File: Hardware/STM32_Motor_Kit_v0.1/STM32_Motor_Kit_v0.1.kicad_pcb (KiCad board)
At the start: 4 copper layers, 150 x 100 mm, 376 parts, among them J1 Conn_01x02_Male, J2 Conn_02x04_Odd_Even, J3 Conn_01x02_Male, J4 Conn_01x03_Male, J5 Conn_01x05_Male, J6 Conn_02x09_Odd_Even, J7 Conn_01x02_Male, J8 USB_B_Mini, Q1 NTMFS4119NT1G, Q2 NTMFS4119NT1G, Q3 NTMFS4119NT1G, Q4 NTMFS4119NT1G, Q5 NTMFS4119NT1G, Q6 NTMFS4119NT1G, Q7 MMUN2235LT1G, SW1 SW_DIP_x01, SW2 Push_Button_SMD_4P, SW3 Push_Button_SMD_4P, U1 STM32G431RBT6, U10 LMV358IDRG4, U11 LMV358IDRG4, U12 LMV358IDRG4, U13 LSF0204DPWR, U14 THVD1500D, U15 SN74HC595DRG3, U16 M24C64-WMN6TP, U17 TVS_Diode_USB, U2 AMS111733TR-HT, U3 LMV358IDRG4, U4 TPS54331DR, U5 MC78M15CDTRKG-, U6 TJA1441BT_0Z, U7 IR2104STRPBF, U8 IR2104STRPBF, U9 IR2104STRPBF, Y1 CRYSTAL_8mHz

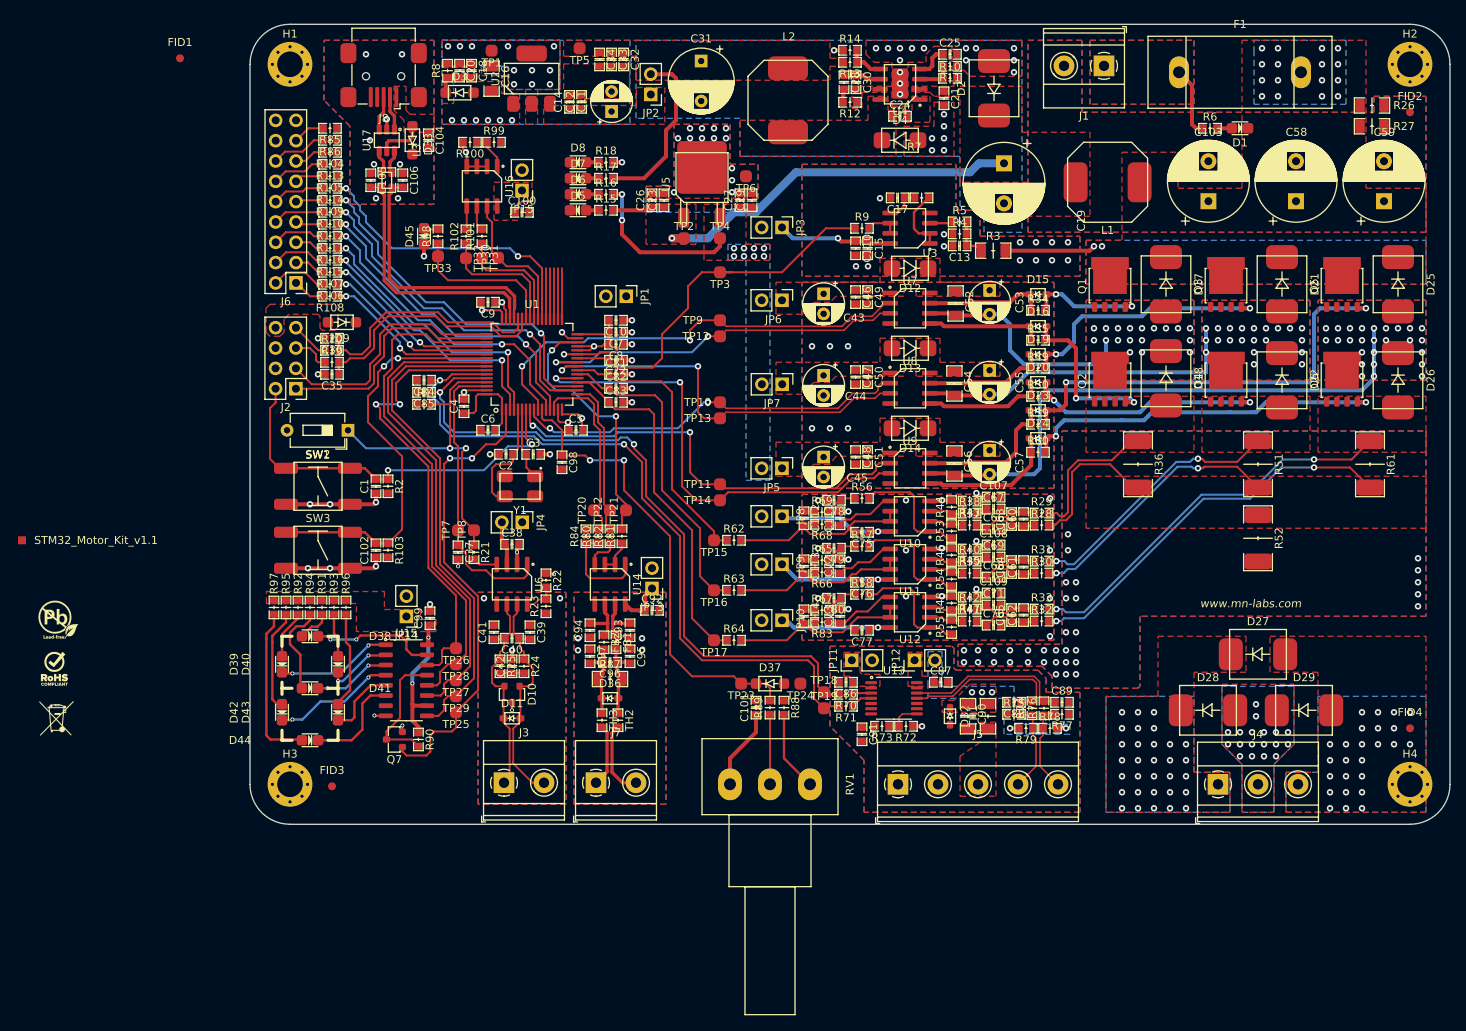
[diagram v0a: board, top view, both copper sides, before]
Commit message: 26.08.2024
1nF 2KV chassis ile GND arasına ekledim. PCB'de güncellemeler oldu.
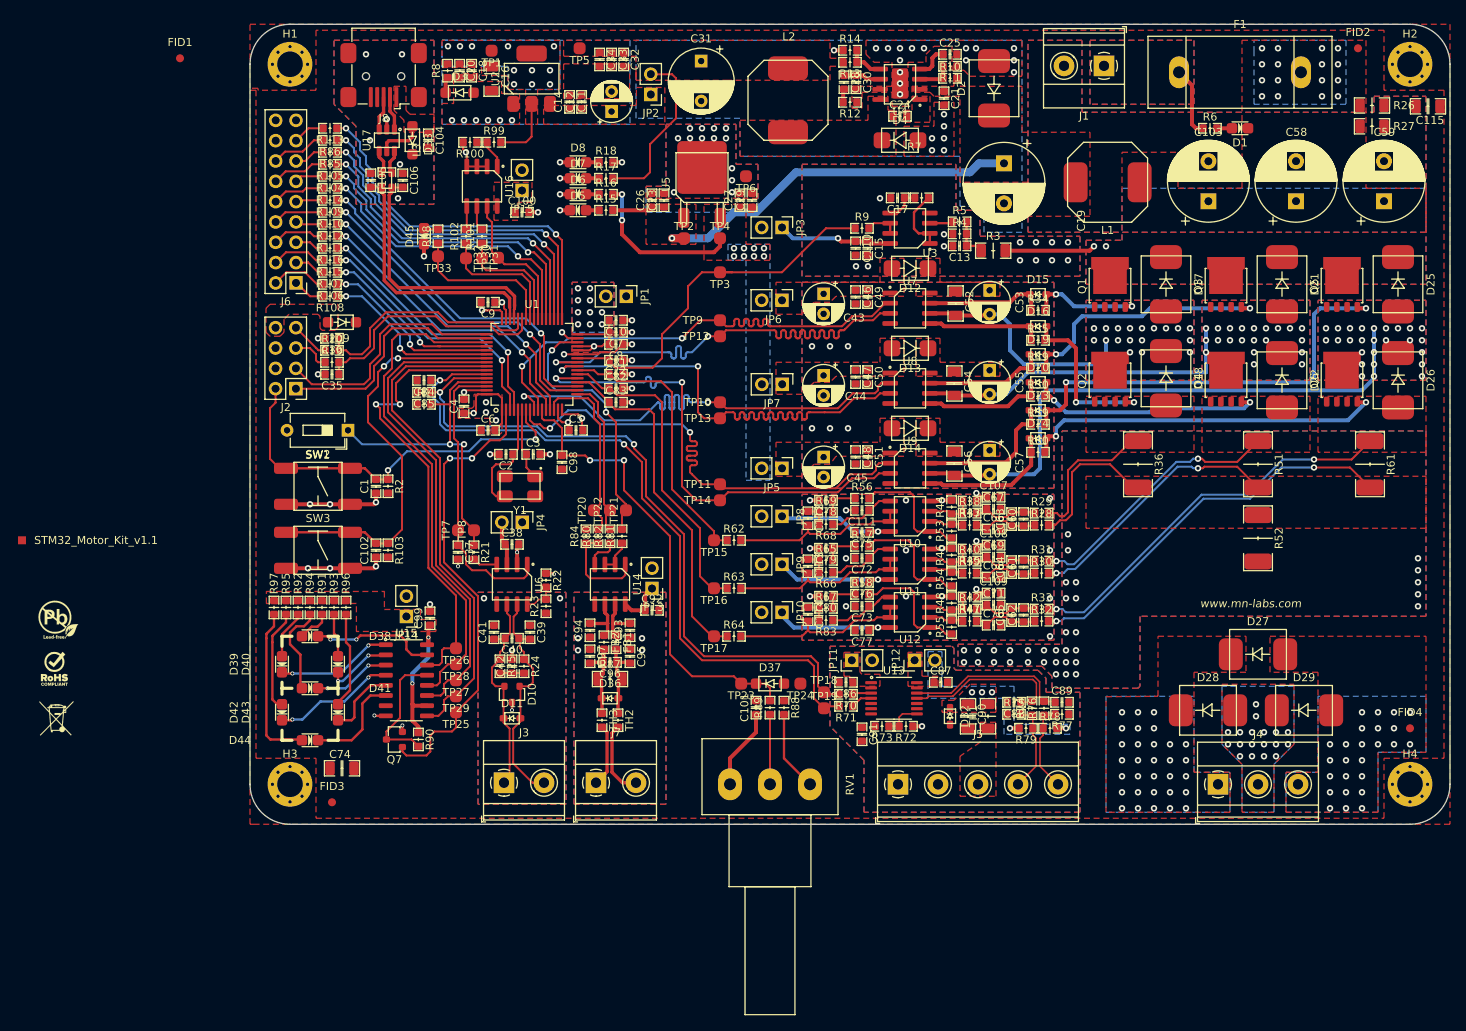
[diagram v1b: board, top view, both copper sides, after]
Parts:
- added C115: 1nF_2KV, AKE_Capacitor_SMD:CAP_1206, F.Cu at (197.2, 60.2)
- added C74: 1nF_2KV, AKE_Capacitor_SMD:CAP_1206, F.Cu at (61.5, 143.0)
- moved FID2 10.3 mm to (188.5, 53.0)
- moved R113 4.50 mm to (60.0, 63.0)
- moved C73 3.02 mm to (126.5, 122.8), turned to 180 degrees
- moved R104 3.00 mm to (60.0, 69.0)
- moved R85 3.00 mm to (60.0, 66.0)
- moved C111 2.93 mm to (126.5, 110.8), turned to 180 degrees
- moved C72 2.93 mm to (126.5, 116.8), turned to 180 degrees
- moved FID3 2.00 mm to (60.2, 147.2)
- moved R105 1.50 mm to (60.0, 67.5)
- moved C80 1.03 mm to (122.0, 121.5)
- moved C78 1.00 mm to (122.0, 109.5)
- moved C79 1.00 mm to (122.0, 115.5)
- moved JP10 1.00 mm to (116.5, 123.5)
- moved C114 0.56 mm to (119.8, 123.8)
- moved R67 0.56 mm to (122.0, 123.0)
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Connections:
- H1 pad 1: unconnected-(H1-Pad1) -> Chassis
- H2 pad 1: unconnected-(H2-Pad1) -> Chassis
- H3 pad 1: unconnected-(H3-Pad1) -> Chassis
- H4 pad 1: unconnected-(H4-Pad1) -> Chassis
- R104 pad 2: /GPIO/Pin_13 -> /GPIO/Pin_11
- R105 pad 1: /MCU/PB12 -> /MCU/PB14
- R105 pad 2: /GPIO/Pin_11 -> /GPIO/Pin_12
- R113 pad 2: /GPIO/Pin_12 -> /GPIO/Pin_15
- R85 pad 2: /GPIO/Pin_15 -> /GPIO/Pin_13
- R86 pad 1: /MCU/PB14 -> /MCU/PB12
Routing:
- net /MCU/PB11: track 6.33 -> 46.3 mm, vias 0 -> 2
- net /MCU/PB12: track 6.33 -> 44.3 mm, vias 0 -> 2
- net /MCU/PB13: track 6.33 -> 42.1 mm, vias 0 -> 2
- net /MCU/PB14: track 6.33 -> 40.3 mm, vias 0 -> 2
- net /MCU/PB15: track 6.33 -> 38.5 mm, vias 0 -> 2
- net /U_Drive_L: track 47.0 -> 61.6 mm
- net /V_Drive_H: track 49.6 -> 61.8 mm
- net /V_Drive_L: track 50.7 -> 61.6 mm
- net +3.3V: track 19.9 -> 28.1 mm
- net /W_Drive_H: track 56.2 -> 61.8 mm
- net /U_Drive_H: track 57.1 -> 61.8 mm
- net GND: track 91.5 -> 95.5 mm, vias 155 -> 158
- net /W_Drive_L: track 59.6 -> 61.8 mm
- net /MCU/PA4: track 43.2 -> 41.9 mm
- net /MCU/PA5: track 44.4 -> 43.1 mm
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- added copper zone on In2.Cu, net +3.3V
- added copper zone on B.Cu, net +3.3V_MCU
- added copper zone on F.Cu, net +3.3V_MCU
- added copper zone on In2.Cu, net +3.3V_MCU
- added copper zone on F.Cu, net Chassis
